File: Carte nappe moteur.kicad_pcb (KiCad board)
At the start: 2 copper layers, 145 x 80 mm, 10 parts, among them J1 Conn_01x03_Male, J2 Conn_01x11_Male, J3 Conn_01x05_Male, J4 Conn_01x03_Male, J5 Conn_01x11_Male, J6 Conn_01x05_Male

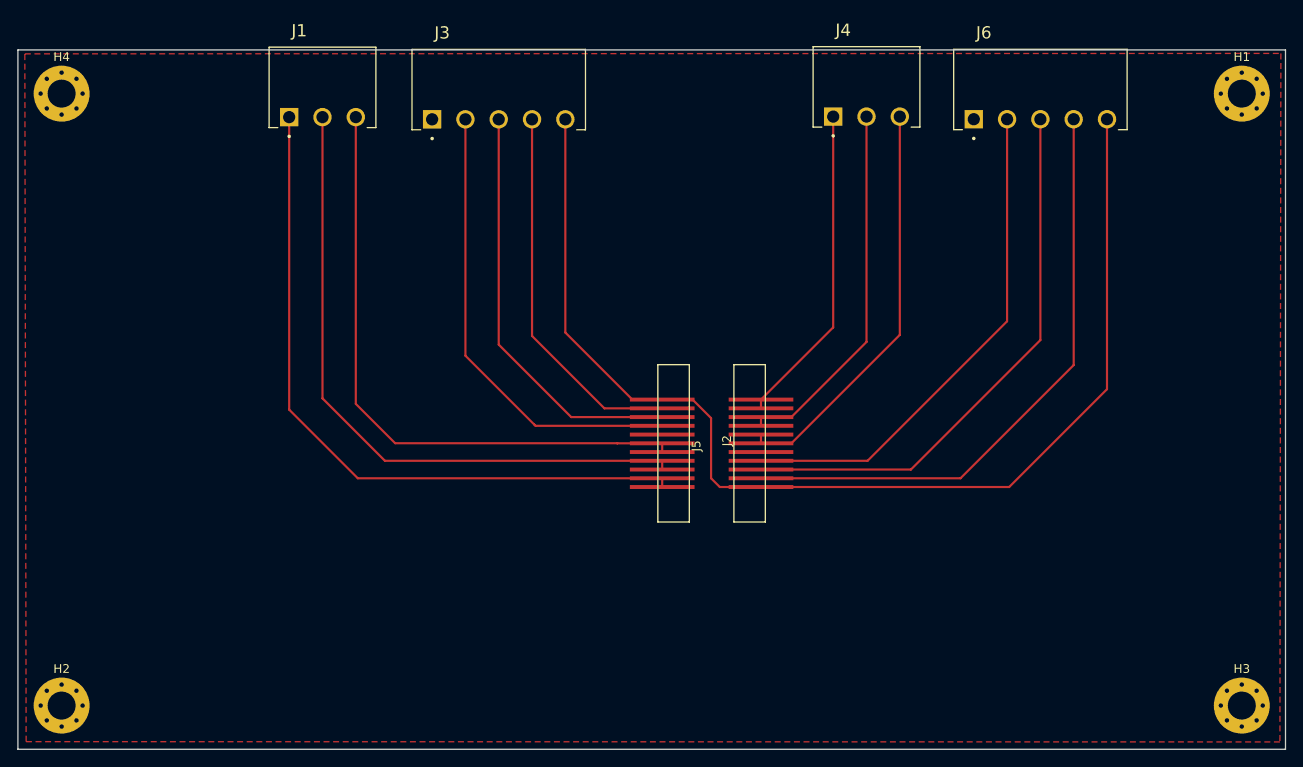
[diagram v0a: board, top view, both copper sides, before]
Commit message: Reduction de la carte pcb
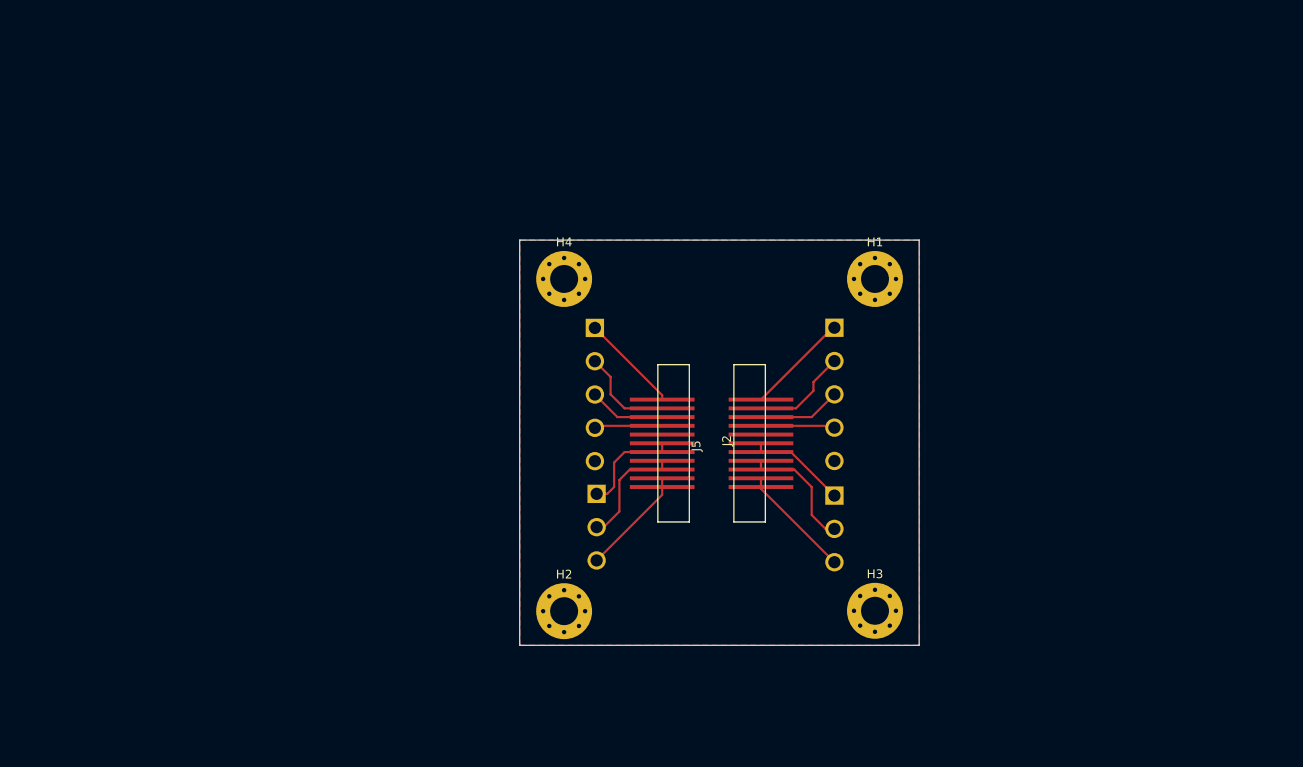
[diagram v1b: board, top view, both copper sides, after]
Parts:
- J1, J3, J4, J6: moved to B.Cu
- moved H4 61.3 mm to (157.5, 76.2)
- moved H? 58.5 mm to (157.5, 114.2)
- moved J1 55.6 mm to (161.2, 100.8), turned to -90 degrees
- moved H1 47.0 mm to (193.0, 76.2)
- moved J4 43.4 mm to (188.4, 101.0), turned to -90 degrees
- moved H3 43.3 mm to (193.0, 114.2)
- moved J3 30.3 mm to (161.0, 81.8), turned to -90 degrees
- moved J6 28.7 mm to (188.4, 81.8), turned to -90 degrees
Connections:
- J2 pad 1: Net-(J1-Pad1) -> Net-(J1-Pad3)
- J2 pad 11: +5V -> Net-(J2-Pad11)
- J2 pad 2: Net-(J1-Pad1) -> Net-(J1-Pad3)
- J2 pad 5: Net-(J1-Pad3) -> Net-(J1-Pad1)
- J2 pad 6: Net-(J1-Pad3) -> Net-(J1-Pad1)
- J3 pad 1: GND -> Net-(J2-Pad11)
- J3 pad 2: Net-(J2-Pad8) -> Net-(J2-Pad10)
- J3 pad 4: Net-(J2-Pad10) -> Net-(J2-Pad8)
- J3 pad 5: +5V -> GND
- J4 pad 1: Net-(J4-Pad1) -> Net-(J5-Pad6)
- J4 pad 3: Net-(J4-Pad3) -> Net-(J5-Pad10)
- J5 pad 1: Net-(J4-Pad1) -> Net-(J5-Pad1)
- J5 pad 11: +5V -> Net-(J5-Pad10)
- J5 pad 2: Net-(J4-Pad1) -> Net-(J6-Pad2)
- J5 pad 3: Net-(J4-Pad2) -> Net-(J6-Pad3)
- J5 pad 4: Net-(J4-Pad2) -> Net-(J6-Pad4)
- J5 pad 5: Net-(J4-Pad3) -> GND
- J5 pad 6: Net-(J4-Pad3) -> Net-(J5-Pad6)
- J5 pad 7: GND -> Net-(J5-Pad6)
- J5 pad 8: Net-(J5-Pad8) -> Net-(J4-Pad2)
- J5 pad 9: Net-(J5-Pad9) -> Net-(J4-Pad2)
- J6 pad 1: GND -> Net-(J5-Pad1)
- J6 pad 2: Net-(J5-Pad8) -> Net-(J6-Pad2)
- J6 pad 3: Net-(J5-Pad9) -> Net-(J6-Pad3)
- J6 pad 4: Net-(J5-Pad10) -> Net-(J6-Pad4)
- J6 pad 5: +5V -> GND
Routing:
- net +5V: track 133.2 -> 0.00 mm
- net Net-(J1-Pad1): track 80.4 -> 12.1 mm
- net Net-(J5-Pad9): track 63.4 -> 0.00 mm
- net Net-(J1-Pad2): track 75.1 -> 13.3 mm
- net Net-(J1-Pad3): track 70.7 -> 12.5 mm
- net Net-(J5-Pad8): track 57.9 -> 0.00 mm
- net Net-(J5-Pad10): track 69.3 -> 13.1 mm
- net Net-(J4-Pad3): track 47.0 -> 0.00 mm
- net Net-(J2-Pad8): track 52.9 -> 7.80 mm
- net Net-(J2-Pad9): track 47.9 -> 8.77 mm
- net Net-(J4-Pad1): track 36.8 -> 0.00 mm
- net Net-(J2-Pad10): track 43.1 -> 11.1 mm
- net Net-(J4-Pad2): track 42.4 -> 14.1 mm
- net Net-(J5-Pad1): track 0.00 -> 11.8 mm
- net Net-(J5-Pad6): track 0.00 -> 11.5 mm
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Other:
- board size 145 x 80 mm -> 45.7 x 46.4 mm

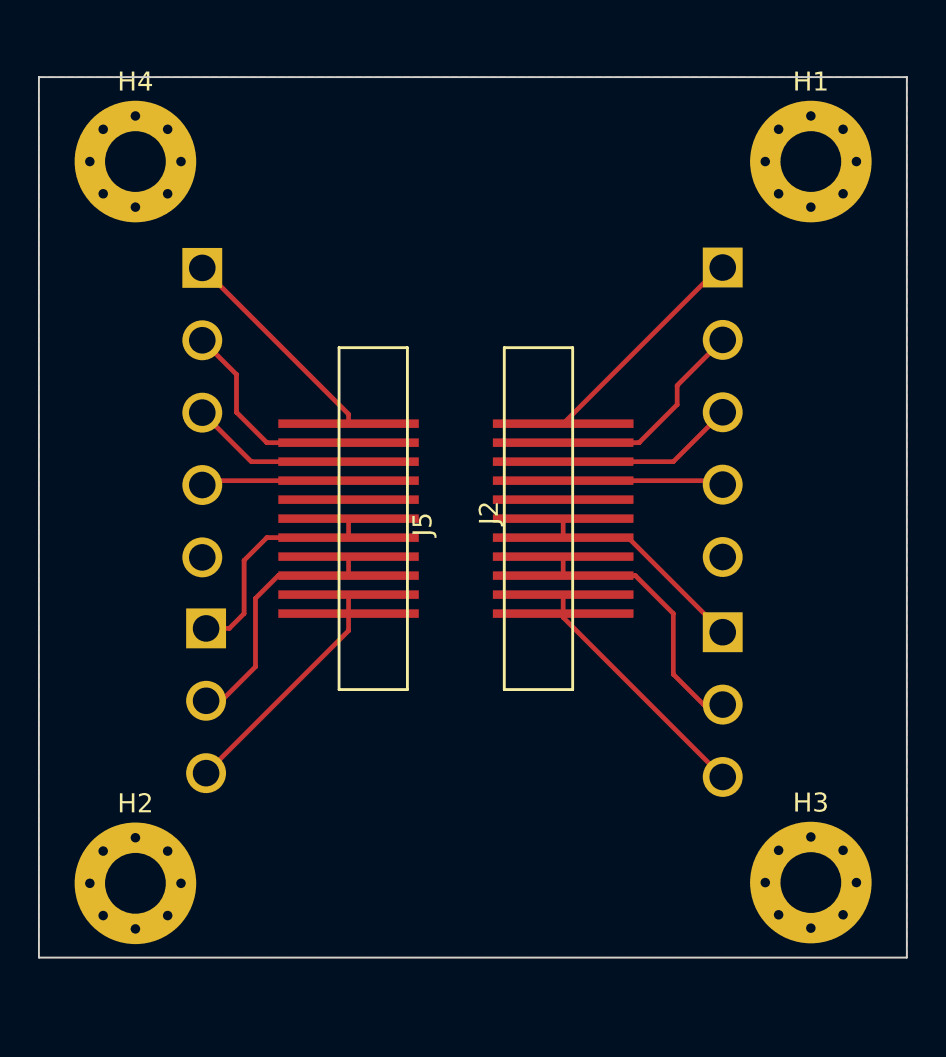
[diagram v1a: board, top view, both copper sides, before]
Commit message: Fix overlap pieces
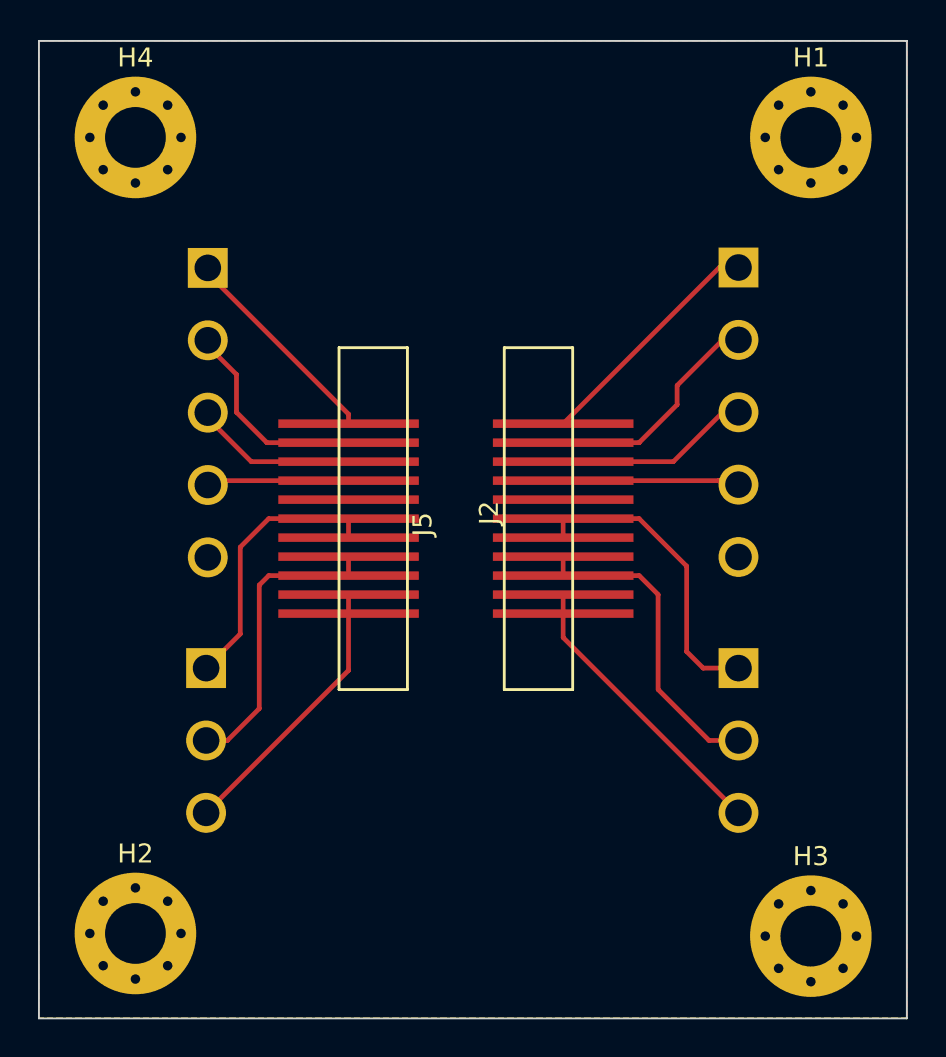
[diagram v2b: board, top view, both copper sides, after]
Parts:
- moved H3 2.82 mm to (193.0, 117.0)
- moved H? 2.64 mm to (157.5, 116.8)
- moved J1 2.09 mm to (161.2, 102.9)
- moved J4 2.06 mm to (189.2, 102.9)
- moved H1 1.27 mm to (193.0, 74.9)
- moved H4 1.27 mm to (157.5, 74.9)
- moved J6 0.83 mm to (189.2, 81.8)
- moved J3 0.29 mm to (161.3, 81.8)
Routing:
- net Net-(J5-Pad6): track 11.5 -> 19.5 mm
- net Net-(J4-Pad2): track 14.1 -> 16.8 mm
- net Net-(J1-Pad2): track 13.3 -> 15.9 mm
- net Net-(J1-Pad1): track 12.1 -> 14.4 mm
- net Net-(J5-Pad10): track 13.1 -> 15.3 mm
- net Net-(J1-Pad3): track 12.5 -> 14.6 mm
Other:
- board size 45.7 x 46.4 mm -> 45.7 x 51.5 mm
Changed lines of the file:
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@@
   (net 15 "Net-(J5-Pad1)")
   (footprint "MountingHole:MountingHole_3.2mm_M3_Pad_Via" (layer "F.Cu")
-    (at 157.48 114.2)
+    (at 157.48 116.84)
     (descr "Mounting Hole 3.2mm, M3")
     (tags "mounting hole 3.2mm m3")
@@
   )
   (footprint "MountingHole:MountingHole_3.2mm_M3_Pad_Via" (layer "F.Cu")
-    (at 193.04 76.2)
+    (at 193.04 74.93)
     (descr "Mounting Hole 3.2mm, M3")
     (tags "mounting hole 3.2mm m3")
@@
   )
   (footprint "MountingHole:MountingHole_3.2mm_M3_Pad_Via" (layer "F.Cu")
-    (at 157.48 76.2)
+    (at 157.48 74.93)
     (descr "Mounting Hole 3.2mm, M3")
     (tags "mounting hole 3.2mm m3")
@@
   )
   (footprint "MountingHole:MountingHole_3.2mm_M3_Pad_Via" (layer "F.Cu")
-    (at 193.04 114.16)
+    (at 193.04 116.98)
     (descr "Mounting Hole 3.2mm, M3")
     (tags "mounting hole 3.2mm m3")
@@
   )
   (footprint "Conn mot block:CUI_TBP02R1-381-03BE" (layer "B.Cu")
-    (at 188.4 100.98 -90)
+    (at 189.23 102.87 -90)
     (property "Sheetfile" "File: Carte nappe moteur.kicad_sch")
     (property "Sheetname" "")
@@
   )
   (footprint "Conn mot block:CUI_TBP02R1-381-05BE" (layer "B.Cu")
-    (at 188.4 81.78 -90)
+    (at 189.23 81.78 -90)
     (property "Sheetfile" "File: Carte nappe moteur.kicad_sch")
     (property "Sheetname" "")
@@
   )
   (footprint "Conn mot block:CUI_TBP02R1-381-03BE" (layer "B.Cu")
-    (at 161.2 100.78 -90)
+    (at 161.2 102.87 -90)
     (property "Sheetfile" "File: Carte nappe moteur.kicad_sch")
     (property "Sheetname" "")
@@
   )
   (footprint "Conn mot block:CUI_TBP02R1-381-05BE" (layer "B.Cu")
-    (at 161 81.8 -90)
+    (at 161.29 81.8 -90)
     (property "Sheetfile" "File: Carte nappe moteur.kicad_sch")
     (property "Sheetname" "")
@@
       (net 1 "GND") (pinfunction "Pin_5") (pintype "passive"))
   )
-  (gr_rect (start 152.4 71.755) (end 198.0946 118.11) (layer "Edge.Cuts") (width 0.1) (fill none))
-  (segment (start 162.42 100.78) (end 161.2 100.78) (width 0.25) (layer "F.Cu") (net 2))
-  (segment (start 168.7 96) (end 164.4 96) (width 0.25) (layer "F.Cu") (net 2))
-  (segment (start 163.2 100) (end 162.42 100.78) (width 0.25) (layer "F.Cu") (net 2))
-  (segment (start 164.4 96) (end 163.2 97.2) (width 0.25) (layer "F.Cu") (net 2))
+  (gr_rect (start 152.4 69.85) (end 198.0946 121.31) (layer "Edge.Cuts") (width 0.1) (fill none))
+  (segment (start 164.5 95) (end 163 96.5) (width 0.25) (layer "F.Cu") (net 2))
+  (segment (start 163 96.5) (end 163 101.07) (width 0.25) (layer "F.Cu") (net 2))
+  (segment (start 163 101.07) (end 161.2 102.87) (width 0.25) (layer "F.Cu") (net 2))
+  (segment (start 168.7 95) (end 164.5 95) (width 0.25) (layer "F.Cu") (net 2))
   (segment (start 168.7 95) (end 168.7 96) (width 0.25) (layer "F.Cu") (net 2))
-  (segment (start 163.2 97.2) (end 163.2 100) (width 0.25) (layer "F.Cu") (net 2))
-  (segment (start 168.7 98) (end 165 98) (width 0.25) (layer "F.Cu") (net 3))
-  (segment (start 163.8 102.8) (end 162.01 104.59) (width 0.25) (layer "F.Cu") (net 3))
-  (segment (start 165 98) (end 163.8 99.2) (width 0.25) (layer "F.Cu") (net 3))
+  (segment (start 164 105) (end 162.32 106.68) (width 0.25) (layer "F.Cu") (net 3))
+  (segment (start 164.5 98) (end 164 98.5) (width 0.25) (layer "F.Cu") (net 3))
+  (segment (start 168.7 98) (end 164.5 98) (width 0.25) (layer "F.Cu") (net 3))
+  (segment (start 162.32 106.68) (end 161.2 106.68) (width 0.25) (layer "F.Cu") (net 3))
   (segment (start 168.7 97) (end 168.7 98) (width 0.25) (layer "F.Cu") (net 3))
-  (segment (start 163.8 99.2) (end 163.8 102.8) (width 0.25) (layer "F.Cu") (net 3))
-  (segment (start 162.01 104.59) (end 161.2 104.59) (width 0.25) (layer "F.Cu") (net 3))
-  (segment (start 168.7 100) (end 168.7 100.9) (width 0.25) (layer "F.Cu") (net 4))
+  (segment (start 164 98.5) (end 164 105) (width 0.25) (layer "F.Cu") (net 3))
   (segment (start 168.7 99) (end 168.7 100) (width 0.25) (layer "F.Cu") (net 4))
-  (segment (start 168.7 100.9) (end 161.2 108.4) (width 0.25) (layer "F.Cu") (net 4))
+  (segment (start 168.7 102.99) (end 161.2 110.49) (width 0.25) (layer "F.Cu") (net 4))
+  (segment (start 168.7 100) (end 168.7 102.99) (width 0.25) (layer "F.Cu") (net 4))
   (segment (start 168.7 92) (end 163.58 92) (width 0.25) (layer "F.Cu") (net 5))
   (segment (start 163.58 92) (end 161 89.42) (width 0.25) (layer "F.Cu") (net 5))
@@
   (segment (start 183.42 96) (end 180 96) (width 0.25) (layer "F.Cu") (net 8))
   (segment (start 180 95) (end 180 96) (width 0.25) (layer "F.Cu") (net 8))
-  (segment (start 188.4 100.98) (end 183.42 96) (width 0.25) (layer "F.Cu") (net 8))
-  (segment (start 180 100.2) (end 188.4 108.6) (width 0.25) (layer "F.Cu") (net 9))
-  (segment (start 180 100) (end 180 100.2) (width 0.25) (layer "F.Cu") (net 9))
+  (segment (start 187.37 102.87) (end 189.23 102.87) (width 0.25) (layer "F.Cu") (net 8))
+  (segment (start 186.5 97.5) (end 186.5 102) (width 0.25) (layer "F.Cu") (net 8))
+  (segment (start 184 95) (end 186.5 97.5) (width 0.25) (layer "F.Cu") (net 8))
+  (segment (start 180 95) (end 184 95) (width 0.25) (layer "F.Cu") (net 8))
+  (segment (start 186.5 102) (end 187.37 102.87) (width 0.25) (layer "F.Cu") (net 8))
+  (segment (start 180 101.26) (end 189.23 110.49) (width 0.25) (layer "F.Cu") (net 9))
+  (segment (start 180 100) (end 180 101.26) (width 0.25) (layer "F.Cu") (net 9))
   (segment (start 180 100) (end 180 99) (width 0.25) (layer "F.Cu") (net 9))
-  (segment (start 185.8 103.2) (end 187.39 104.79) (width 0.25) (layer "F.Cu") (net 10))
+  (segment (start 180 98) (end 184 98) (width 0.25) (layer "F.Cu") (net 10))
+  (segment (start 185 99) (end 185 104) (width 0.25) (layer "F.Cu") (net 10))
   (segment (start 180 98) (end 180 97) (width 0.25) (layer "F.Cu") (net 10))
-  (segment (start 187.39 104.79) (end 188.4 104.79) (width 0.25) (layer "F.Cu") (net 10))
-  (segment (start 183.8 98) (end 185.8 100) (width 0.25) (layer "F.Cu") (net 10))
-  (segment (start 185.8 100) (end 185.8 103.2) (width 0.25) (layer "F.Cu") (net 10))
-  (segment (start 180 98) (end 183.8 98) (width 0.25) (layer "F.Cu") (net 10))
+  (segment (start 187.68 106.68) (end 189.23 106.68) (width 0.25) (layer "F.Cu") (net 10))
+  (segment (start 185 104) (end 187.68 106.68) (width 0.25) (layer "F.Cu") (net 10))
+  (segment (start 184 98) (end 185 99) (width 0.25) (layer "F.Cu") (net 10))
   (segment (start 184 91) (end 186 89) (width 0.25) (layer "F.Cu") (net 11))
   (segment (start 180 91) (end 184 91) (width 0.25) (layer "F.Cu") (net 11))
@@
     (polygon
       (pts
-        (xy 198.12 118.11)
-        (xy 152.4 118.11)
-        (xy 152.4 71.755)
-        (xy 198.12 71.755)
+        (xy 198.12 121.285)
+        (xy 152.4 121.285)
+        (xy 152.4 69.85)
+        (xy 198.12 69.85)
       )
     )

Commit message: Résolution problème de symétrie
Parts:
- moved J6 28.7 mm to (189.2, 110.5), turned to 90 degrees
- moved J4 13.5 mm to (189.2, 89.4), turned to 90 degrees
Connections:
- J4 pad 1: Net-(J5-Pad6) -> Net-(J4-Pad1)
- J4 pad 3: Net-(J5-Pad10) -> Net-(J4-Pad3)
- J5 pad 1: Net-(J5-Pad1) -> Net-(J4-Pad3)
- J5 pad 11: Net-(J5-Pad10) -> Net-(J5-Pad11)
- J5 pad 2: Net-(J6-Pad2) -> Net-(J4-Pad3)
- J5 pad 3: Net-(J6-Pad3) -> Net-(J4-Pad2)
- J5 pad 4: Net-(J6-Pad4) -> Net-(J4-Pad2)
- J5 pad 5: GND -> Net-(J4-Pad1)
- J5 pad 6: Net-(J5-Pad6) -> Net-(J4-Pad1)
- J5 pad 7: Net-(J5-Pad6) -> GND
- J5 pad 8: Net-(J4-Pad2) -> Net-(J5-Pad8)
- J5 pad 9: Net-(J4-Pad2) -> Net-(J5-Pad9)
- J6 pad 1: Net-(J5-Pad1) -> Net-(J5-Pad11)
- J6 pad 2: Net-(J6-Pad2) -> Net-(J5-Pad10)
- J6 pad 3: Net-(J6-Pad3) -> Net-(J5-Pad9)
- J6 pad 4: Net-(J6-Pad4) -> Net-(J5-Pad8)
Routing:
- net Net-(J5-Pad6): track 19.5 -> 0.00 mm
- net Net-(J4-Pad3): track 0.00 -> 15.0 mm
- net Net-(J5-Pad11): track 0.00 -> 14.3 mm
- net Net-(J4-Pad1): track 0.00 -> 12.1 mm
- net Net-(J5-Pad1): track 11.8 -> 0.00 mm
- net Net-(J5-Pad9): track 0.00 -> 11.2 mm
- net Net-(J6-Pad2): track 11.2 -> 0.00 mm
- net Net-(J5-Pad8): track 0.00 -> 10.1 mm
- net Net-(J6-Pad3): track 9.48 -> 0.00 mm
- net Net-(J6-Pad4): track 8.49 -> 0.00 mm
- net Net-(J4-Pad2): track 16.8 -> 13.5 mm
- net Net-(J5-Pad10): track 15.3 -> 13.7 mm
